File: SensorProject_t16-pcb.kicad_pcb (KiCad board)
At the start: 2 copper layers, 48.3 x 71.1 mm, 90 parts, among them J1 Conn_01x02_Pin, J10 Conn_01x02_Pin, J11 Conn_01x02_Pin, J12 Conn_01x02_Pin, J13 Conn_01x02_Pin, J14 Conn_01x02_Pin, J15 Conn_01x02_Pin, J16 Conn_01x02_Pin, J17 Conn_01x04_Socket, J18 THTPad, J2 Conn_01x02_Pin, J20 Screw_Terminal_01x02, J21 Conn_2x02_Pin, J3 Conn_01x02_Pin, J4 Conn_01x02_Pin, J5 Conn_01x02_Pin, J6 Conn_01x02_Pin, J7 Conn_01x02_Pin, J8 Conn_01x02_Pin, J9 Conn_01x02_Pin, SW1 SW_Push, SW2 SW_Push, U1 ADS1115IDGS, U2 ADS1115IDGS, U3 ADS1115IDGS, U4 ADS1115IDGS, U5 STM32F411CEUx, U6 AMS1117-3.3, U7 RFM95W-915S2, Y1 25MHz, Y2 32.758kHz

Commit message: As made,  t16-F411 v0.2.0 2025-05, with added notes about needed fixes and results from some testing.
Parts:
- D1: value red -> red 2ma 2.65Vf
- D2: value blue -> blue 2ma 2.65Vf
- D3: value BAT54C -> BAT54C-HF
- R23: value 400 -> 698
- R24: value 100 -> 274
- U5: value STM32F411CEUx -> STM32F411CEU6
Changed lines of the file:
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@@
 			(drillshape 0)
 			(scaleselection 1)
-			(outputdirectory "./outputs")
+			(outputdirectory "Private/Sunsel-submit_2025-05/v2/gerber_2025_05_22/")
 		)
 	)
@@
 			)
 		)
-		(property "Description" "Ultra-Small, Low-Power, I2C-Compatible, 860-SPS, 16-Bit ADCs With Internal Reference, Oscillator, and Programmable Comparator, VSSOP-10"
+		(property "Description" "Low-Power ADCs, I2C-Compatible, 16-Bit , VSSOP-10"
 			(at 0 0 270)
 			(unlocked yes)
@@
 			)
 		)
-		(property "Description" "Ultra-Small, Low-Power, I2C-Compatible, 860-SPS, 16-Bit ADCs With Internal Reference, Oscillator, and Programmable Comparator, VSSOP-10"
+		(property "Description" "Low-Power ADCs, I2C-Compatible, 16-Bit , VSSOP-10"
 			(at 0 0 270)
 			(unlocked yes)
@@
 			)
 		)
-		(property "Value" "BAT54C"
+		(property "Value" "BAT54C-HF"
 			(at 0 2.4 90)
 			(layer "F.Fab")
@@
 			)
 		)
-		(property "Datasheet" "http://www.diodes.com/_files/datasheets/ds11005.pdf"
+		(property "Datasheet" "https://www.comchiptech.com/admin/files/product/QW-JB083%20BAT54-HF%20Series%20RevA.pdf"
 			(at 0 0 90)
 			(layer "F.Fab")
@@
 			)
 		)
-		(property "Manufacturer" "Diodes Inc."
+		(property "Manufacturer" "Comchip Technology"
 			(at 0 0 90)
 			(unlocked yes)
@@
 			)
 		)
-		(property "MfgPart" "BAT54C"
+		(property "MfgPart" "BAT54C-HF"
 			(at 0 0 90)
 			(unlocked yes)
@@
 			)
 		)
-		(property "Value" "STM32F411CEUx"
+		(property "Value" "STM32F411CEU6"
 			(at 0 4.83 135)
 			(layer "F.Fab")
@@
 			)
 		)
-		(property "Description" "STMicroelectronics Arm Cortex-M4 MCU, 512KB flash, 128KB RAM, 100 MHz, 1.7-3.6V, 36 GPIO, UFQFPN48"
+		(property "Description" "Arm Cortex-M4 MCU, 512KB flash, 128KB RAM,  1.7-3.6V, UFQFPN48"
 			(at 0 0 135)
 			(layer "F.Fab")
@@
 			)
 		)
-		(property "MfgPart" "STM32F411CEUx"
+		(property "MfgPart" "STM32F411CEU6"
 			(at 0 0 315)
 			(unlocked yes)
@@
 			)
 		)
-		(property "Description" "Ultra-Small, Low-Power, I2C-Compatible, 860-SPS, 16-Bit ADCs With Internal Reference, Oscillator, and Programmable Comparator, VSSOP-10"
+		(property "Description" "Low-Power ADCs, I2C-Compatible, 16-Bit , VSSOP-10"
 			(at 0 0 270)
 			(unlocked yes)
@@
 			)
 		)
-		(property "Value" "blue"
-			(at -0.02 -1.5 0)
+		(property "Value" "blue 2ma 2.65Vf"
+			(at -1.21 -0.54 0)
 			(layer "F.Fab")
 			(effects
@@
 			)
 		)
-		(property "Datasheet" ""
+		(property "Datasheet" "https://www.kingbrightusa.com/images/catalog/SPEC/APHD1608LVBC-D.pdf"
 			(at 0 0 0)
 			(unlocked yes)
@@
 			)
 		)
-		(property "Manufacturer" "Yongyu Photoelectric"
+		(property "Manufacturer" "Kingbright"
 			(at 0 0 0)
 			(unlocked yes)
@@
 			)
 		)
-		(property "MfgPart" "yy0603bl-nn1s0-t2ar4"
+		(property "MfgPart" "APHD1608LVBC/D"
 			(at 0 0 0)
 			(unlocked yes)
@@
 			)
 		)
-		(property "Description" "Ultra-Small, Low-Power, I2C-Compatible, 860-SPS, 16-Bit ADCs With Internal Reference, Oscillator, and Programmable Comparator, VSSOP-10"
+		(property "Description" "Low-Power ADCs, I2C-Compatible, 16-Bit , VSSOP-10"
 			(at 0 0 270)
 			(unlocked yes)
@@
 			)
 		)
-		(property "Value" "red"
-			(at 0 1.43 0)
+		(property "Value" "red 2ma 2.65Vf"
+			(at 0.68 0.48 0)
 			(layer "F.Fab")
 			(effects
@@
 			)
 		)
-		(property "Datasheet" ""
+		(property "Datasheet" "https://www.digikey.cn/en/products/detail/kingbright/APTD1608LSECK-J3-PF/5177446"
 			(at 0 0 0)
 			(unlocked yes)
@@
 			)
 		)
-		(property "Manufacturer" "Yongyu Photoelectric"
+		(property "Manufacturer" "Kingbright"
 			(at 0 0 0)
 			(unlocked yes)
@@
 			)
 		)
-		(property "MfgPart" "yy0603re-nn1s0-t2ar4"
+		(property "MfgPart" "APTD1608LSECK-J3-PF"
 			(at 0 0 0)
 			(unlocked yes)
@@
 			)
 		)
-		(property "Value" "100"
+		(property "Value" "274"
 			(at 0 1.43 0)
 			(layer "F.Fab")
@@
 			)
 		)
-		(property "Description" "Generic screw terminal, single row, 01x02, script generated (kicad-library-utils/schlib/autogen/connector/)"
+		(property "Description" "Generic screw terminal, 01x02"
 			(at 0 0 180)
 			(unlocked yes)
@@
 			)
 		)
-		(property "Value" "400"
+		(property "Value" "698"
 			(at 0 -1.43 180)
 			(layer "B.Fab")
@@
 		(sheetname "/RFM95W/")
 		(sheetfile "RFM95W.kicad_sch")
-		(attr through_hole)
+		(attr through_hole dnp)
 		(fp_line
 			(start 0 1.33)
@@
 			)
 		)
-		(property "Description" "Low power long range transceiver module, SPI and parallel interface, 915 MHz, spreading factor 6 to12, bandwidth 7.8 to 500kHz, -111 to -148 dBm, SMD-16, DIP-16"
+		(property "Description" "LoRa module, SPI, 915 MHz"
 			(at 0 0 90)
 			(unlocked yes)

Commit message: Most post v0.2.0 fixes done. About to mess with GND_ANT zone and net.
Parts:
- added R31: 10k 1%, ProjectLib:R_0603_1608Metric, F.Cu at (91.1, 48.3)
- added R32: 10k 1%, ProjectLib:R_0603_1608Metric, F.Cu at (95.0, 57.4)
- AE1: value 915mhz antenna -> Antenna_Shield; footprint ProjectLib:915MHz_spring_antenna -> ProjectLib:U.FL_Molex_MCRF_73412-0110_Vertical
- J18: value THTPad -> a8 MCO
- SW1: value SW_Push -> RST
- SW2: value SW_Push -> BT0
- U6: value AMS1117-3.3 -> AMS1117-3.3 SOT-223
- moved AE1 2.73 mm to (95.0, 87.0), turned to 90 degrees
- moved L1 0.20 mm to (75.3, 53.2)
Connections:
- net /f411/LSE/GND_LSE renamed GND_LSE
- J17 pad 3: SCL2 -> SCL1
- J17 pad 4: SDA2 -> SDA1
- R17 pad 2: SCL1 -> SCL2
- R18 pad 2: SDA1 -> SDA2
- U1 pad 10: SCL1 -> SCL2
- U1 pad 9: SDA1 -> SDA2
- U2 pad 10: SCL1 -> SCL2
- U2 pad 9: SDA1 -> SDA2
- U3 pad 1: SDA1 -> SDA2
- U3 pad 10: SCL1 -> SCL2
- U3 pad 9: SDA1 -> SDA2
- U4 pad 1: SCL1 -> SCL2
- U4 pad 10: SCL1 -> SCL2
- U4 pad 9: SDA1 -> SDA2
- U5 pad 21: SCL1 -> SCL2
- U5 pad 39: SDA1 -> SDA2
- U5 pad 42: SDA2 -> unconnected-(U5-PB6-Pad42)
- U5 pad 45: SCL2 -> SCL1
- U5 pad 46: unconnected-(U5-PB9-Pad46) -> SDA1
- U6 pad 4: GND -> +3V3
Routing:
- net SDA2: track 9.74 -> 73.2 mm, vias 0 -> 2
- net SCL1: track 65.7 -> 10.3 mm, vias 5 -> 0
- net SCL2: track 10.3 -> 65.7 mm, vias 0 -> 5
- net SDA1: track 73.2 -> 18.1 mm, vias 2 -> 0
- net +3V3: track 401.2 -> 415.6 mm
- net GND: track 65.1 -> 58.2 mm
- net Net-(AE1-A): track 4.71 -> 2.79 mm
- net Net-(U5-BOOT0): track 18.7 -> 20.2 mm
- net VBAT: track 21.8 -> 20.9 mm
- net Net-(D2-K): track 13.9 -> 13.0 mm
- added copper zone on B.Cu, net (none)
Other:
- board text added: "915MHz"
- board text added: "CR1216 3v"
- board text added: "SDA1"
- board text added: "SLC1"
- board text added: "b8"
- board text added: "b9"
- board text removed: "SDA2"
- board text removed: "SLC2"

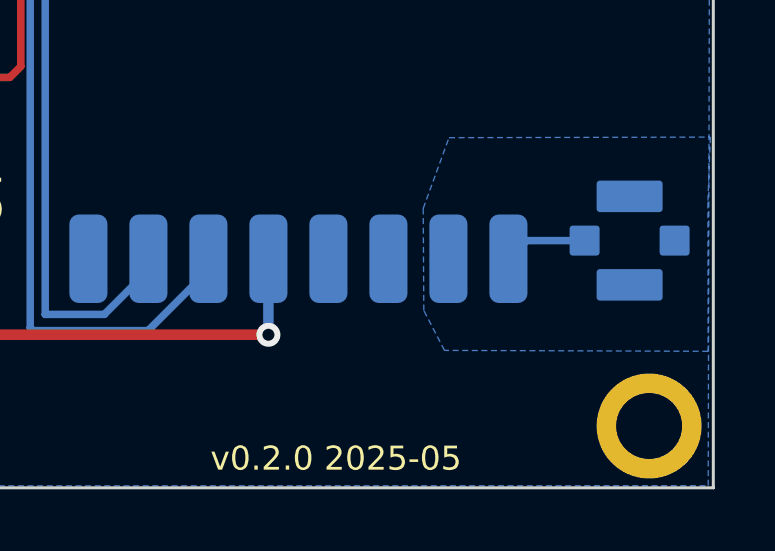
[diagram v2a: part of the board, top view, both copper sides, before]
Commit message: Added U.FL for antenna, with GND_ANT zone.
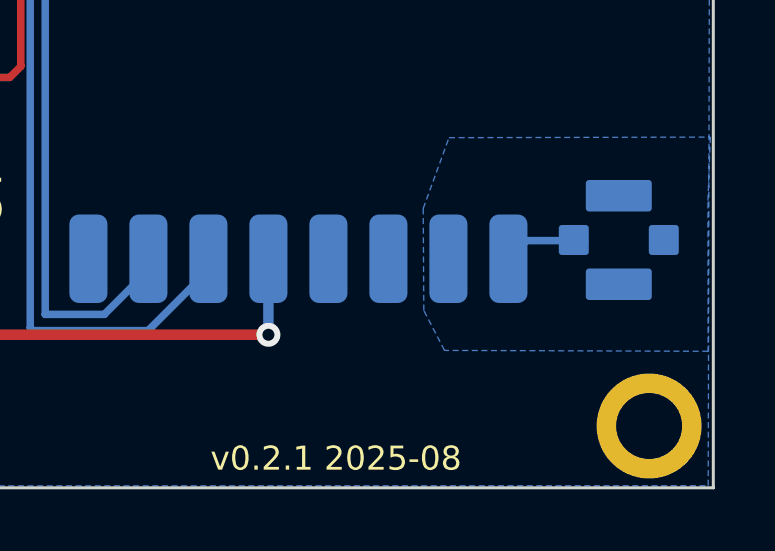
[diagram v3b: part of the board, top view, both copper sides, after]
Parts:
- AE1: value Antenna_Shield -> U.FL
- moved AE1 0.36 mm to (94.6, 87.0)
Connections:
- AE1 pad 2: GND -> GND_ANT
- U7 pad 10: GND -> GND_ANT
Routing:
- added copper zone on B.Cu, net GND_ANT
- removed copper zone on B.Cu, net (none)
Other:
- board text added: "v0.2.1 2025-08"
- board text removed: "v0.2.0 2025-05"

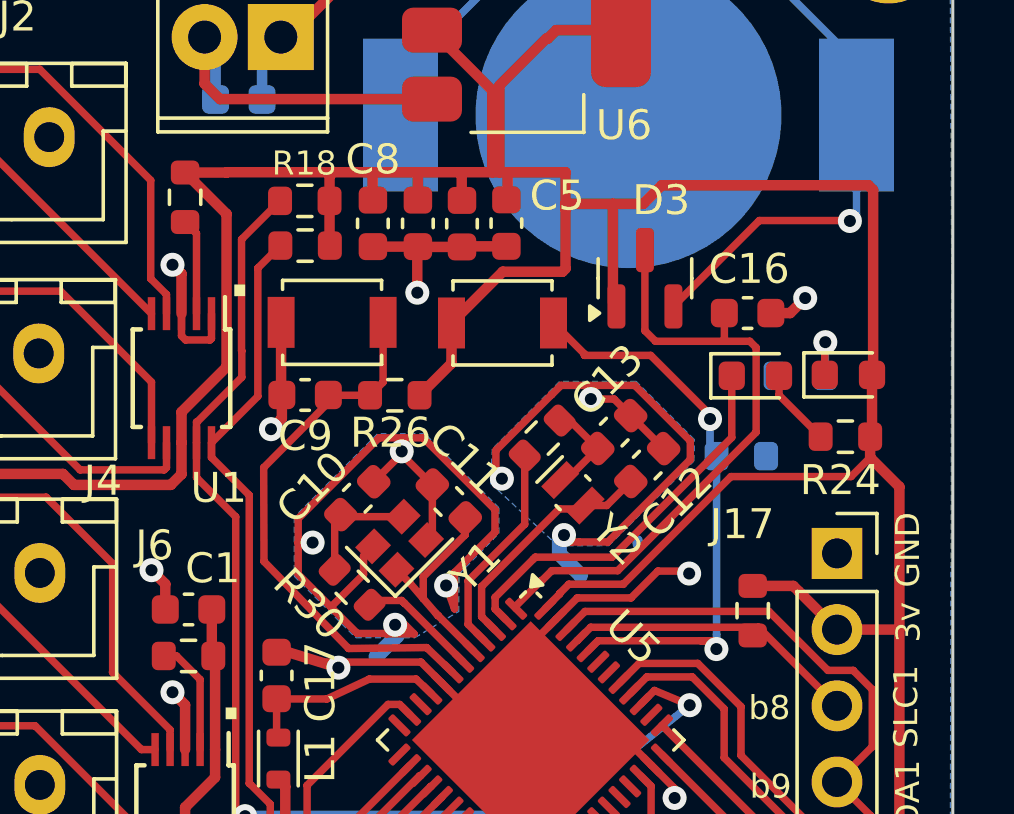
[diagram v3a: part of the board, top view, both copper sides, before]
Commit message: BOM cleaned up.
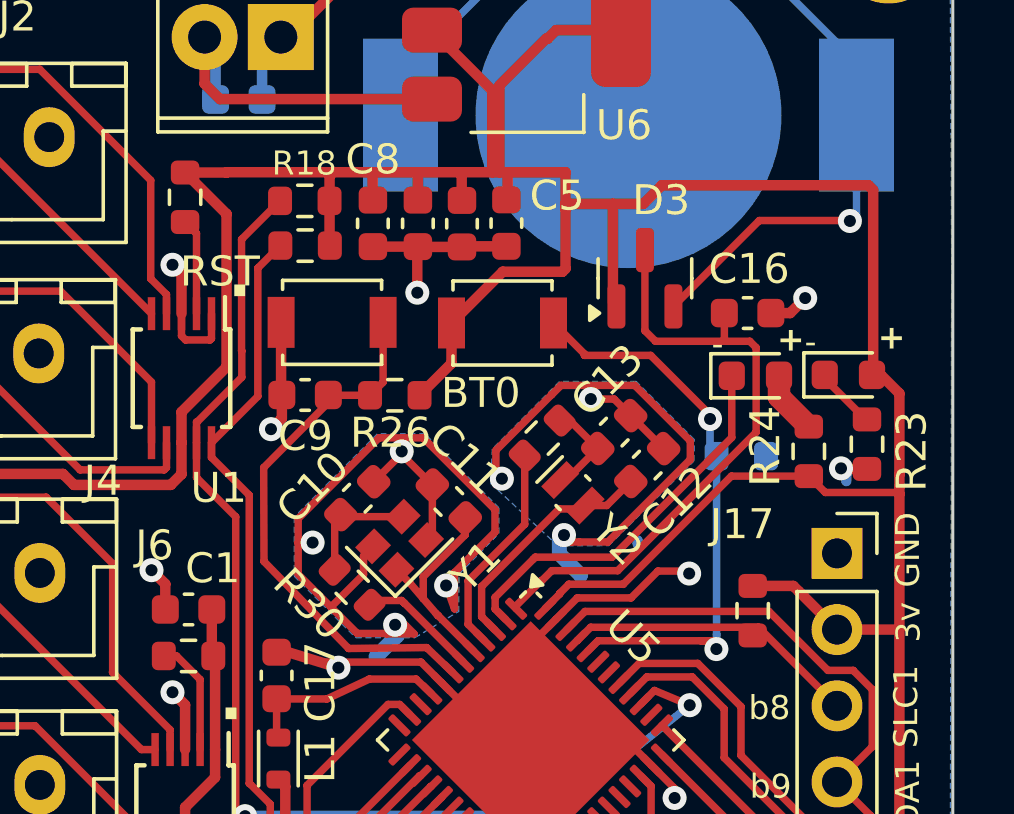
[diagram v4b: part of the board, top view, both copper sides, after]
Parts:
- D1: value red 2ma 2.65Vf -> red 2ma 1.8Vf
- R23: moved to F.Cu
- SW1: value RST -> SW_Push
- SW2: value BT0 -> SW_Push
- moved R23 3.19 mm to (94.9, 42.7), turned to -90 degrees
- moved R24 1.31 mm to (93.0, 43.0), turned to 90 degrees
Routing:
- net GND: track 58.2 -> 59.6 mm, vias 17 -> 18
- net +3V3: track 415.6 -> 416.6 mm
- net Net-(D1-K): track 2.21 -> 1.95 mm, vias 1 -> 0
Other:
- board text added: "-"
- board text added: "BT0"
- board text added: "RST"

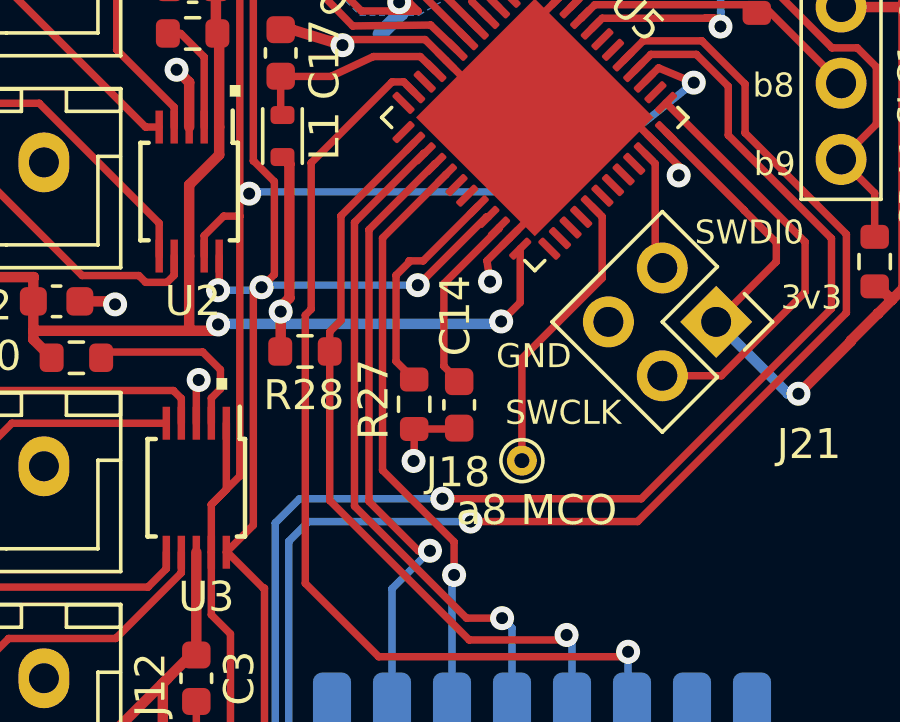
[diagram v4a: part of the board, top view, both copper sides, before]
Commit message: added test pad access to PB2 for boot1, renames J18 to TP2.
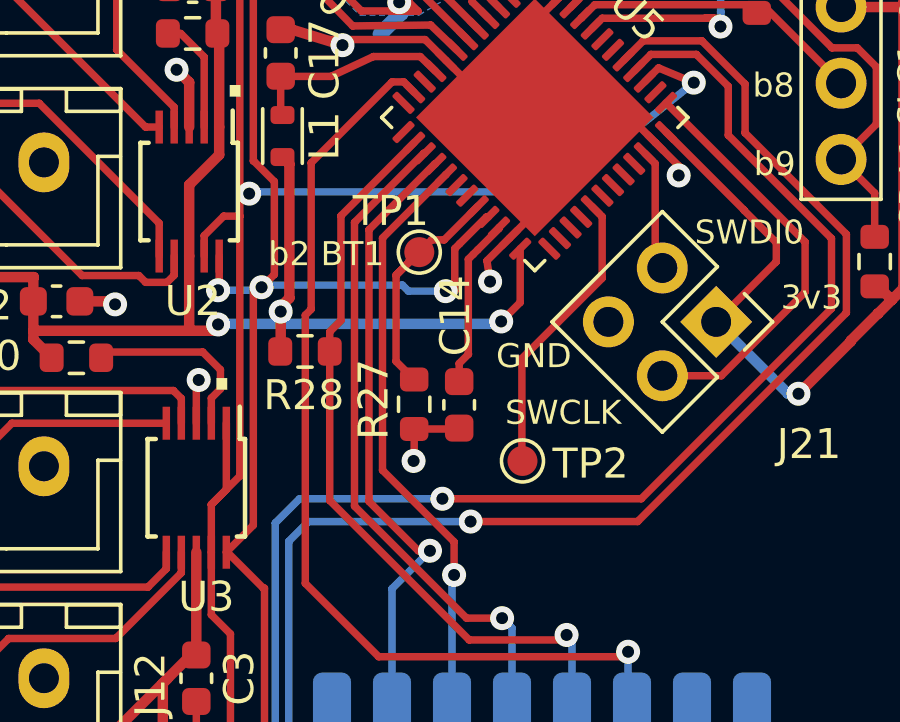
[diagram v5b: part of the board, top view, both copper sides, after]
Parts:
- removed J18: a8 MCO, ProjectLib:TestPoint_THTPad_D1.0mm_Drill0.5mm
- added TP1: BT1 b2, ProjectLib:TestPoint_Pad_D1.0mm, F.Cu at (79.9, 57.1)
- added TP2: a8 MCO, ProjectLib:TestPoint_Pad_D1.0mm, F.Cu at (83.3, 64.0)
- R23: value 698 -> 715 1%
- R24: value 274 -> 280 1%
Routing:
- net Net-(U5-PB2): track 7.43 -> 8.53 mm
- net SCL2: track 65.7 -> 66.7 mm
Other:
- board text added: "b2 BT1"

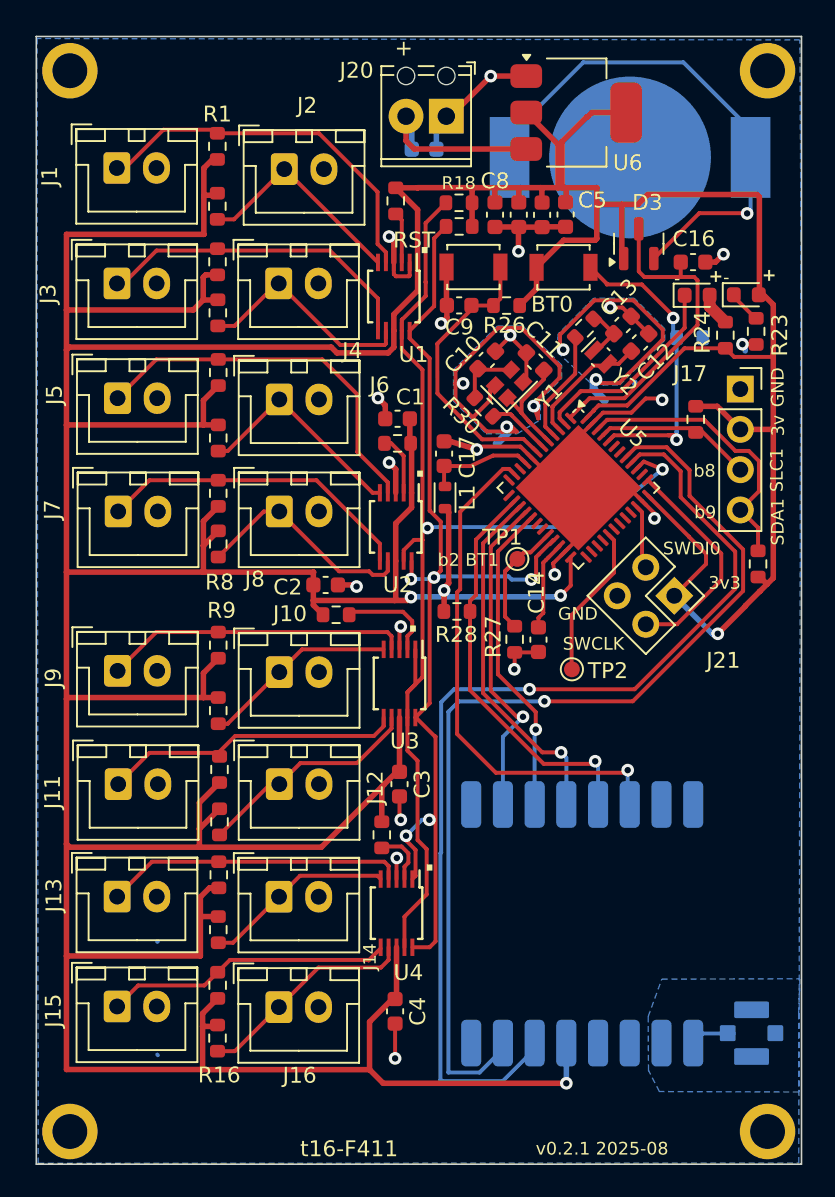
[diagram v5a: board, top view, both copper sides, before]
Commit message: flip side for radio in progress.
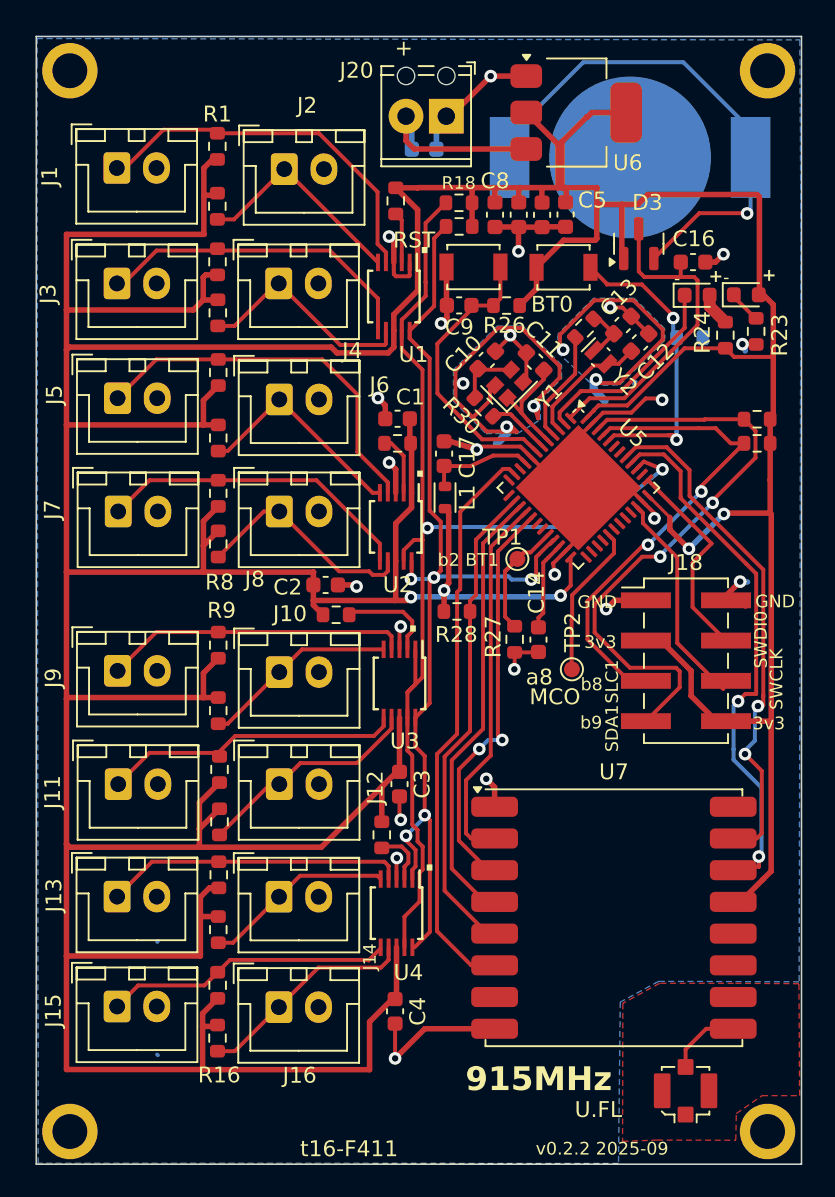
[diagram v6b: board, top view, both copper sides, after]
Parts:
- removed J17: Conn_01x04_Socket, ProjectLib:PinSocket_1x04_P2.54mm_Vertical
- removed J21: Conn_2x02_Pin, ProjectLib:PinSocket_2x02_P2.54mm_Vertical
- removed R31, R32: 10k 1%, ProjectLib:R_0603_1608Metric
- added J18: Conn_02x04_Top_Bottom, ProjectLib:PinHeader_2x04_P2.54mm_Vertical_SMD, F.Cu at (90.5, 63.5)
- added R33: 10k 1%, ProjectLib:R_0603_1608Metric, F.Cu at (95.0, 49.8)
- added R34: 10k 1%, ProjectLib:R_0603_1608Metric, F.Cu at (95.0, 48.3)
- AE1, U7: moved to F.Cu
- TP2: value a8 MCO -> MCO
- moved AE1 5.52 mm to (90.5, 90.6), turned to 180 degrees
- moved U7 2.04 mm to (86.0, 79.7), turned to 0 degrees
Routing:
- net DIO1: track 62.5 -> 33.0 mm, vias 1 -> 2
- net DIO0: track 64.8 -> 35.4 mm, vias 1 -> 2
- net SCL1: track 10.3 -> 30.9 mm, vias 0 -> 2
- net SDA1: track 18.1 -> 38.5 mm, vias 0 -> 2
- net GND: track 59.6 -> 73.4 mm, vias 18 -> 21
- net /f411/SWDIO: track 3.73 -> 14.3 mm
- net MOSI: track 20.0 -> 26.0 mm, vias 1 -> 2
- net SCK: track 22.6 -> 28.2 mm, vias 1 -> 0
- net NSS: track 25.8 -> 30.7 mm, vias 1 -> 0
- net RESET: track 32.7 -> 36.3 mm, vias 1 -> 0
- net MISO: track 20.9 -> 23.8 mm, vias 1 -> 0
- net +3V3: track 416.6 -> 418.9 mm
- net Net-(AE1-A): track 2.79 -> 4.65 mm
- net SCL2: track 66.7 -> 65.3 mm
- net /f411/SWCLK: track 14.1 -> 13.2 mm
- added copper zone on F.Cu, net GND_ANT
- removed copper zone on B.Cu, net GND_ANT
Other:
- board text added: "a8"
- board text added: "v0.2.2 2025-09"
- board text removed: "3v"
- board text removed: "v0.2.1 2025-08"
